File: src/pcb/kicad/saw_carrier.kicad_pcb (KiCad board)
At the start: 2 copper layers, 60.5 x 19.5 mm, 16 parts, among them J1 Conn_Coaxial, J2 Conn_Coaxial, U1 SAW_Sensor

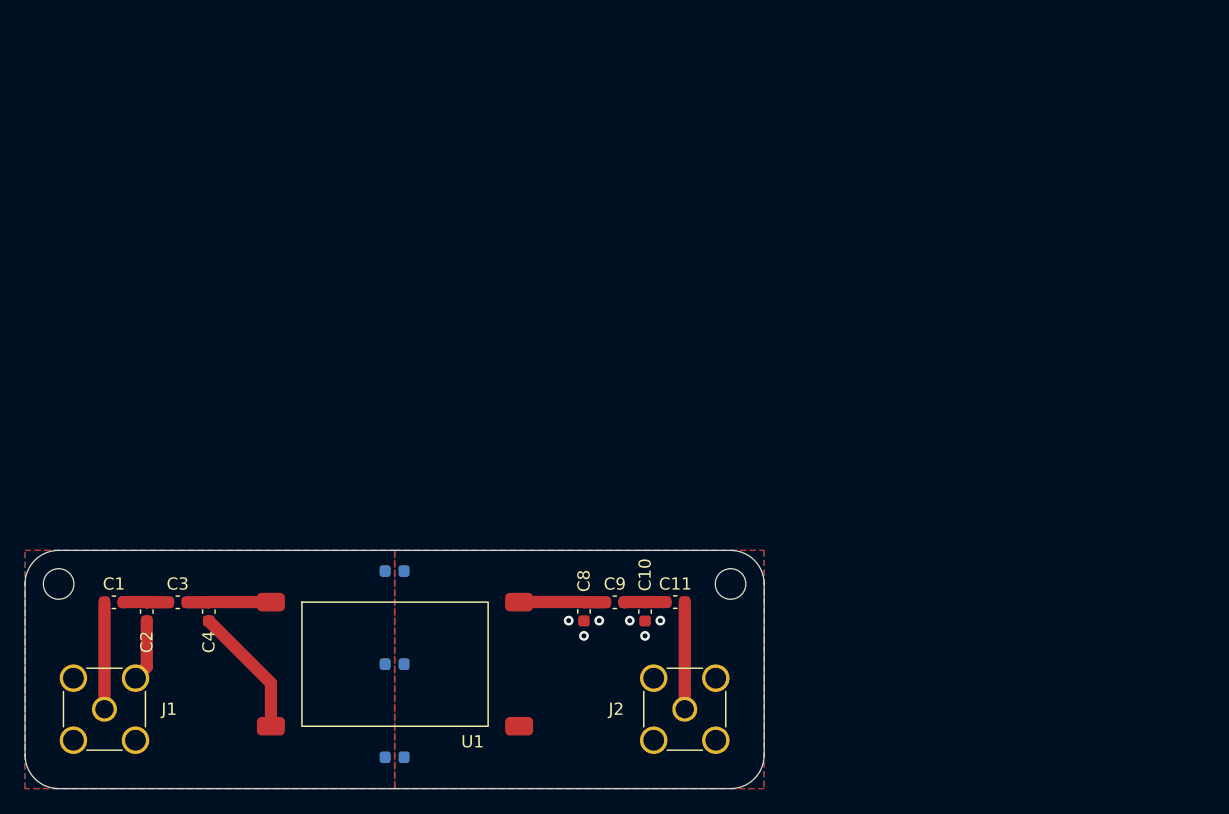
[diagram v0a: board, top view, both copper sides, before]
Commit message: remove obsolete folder
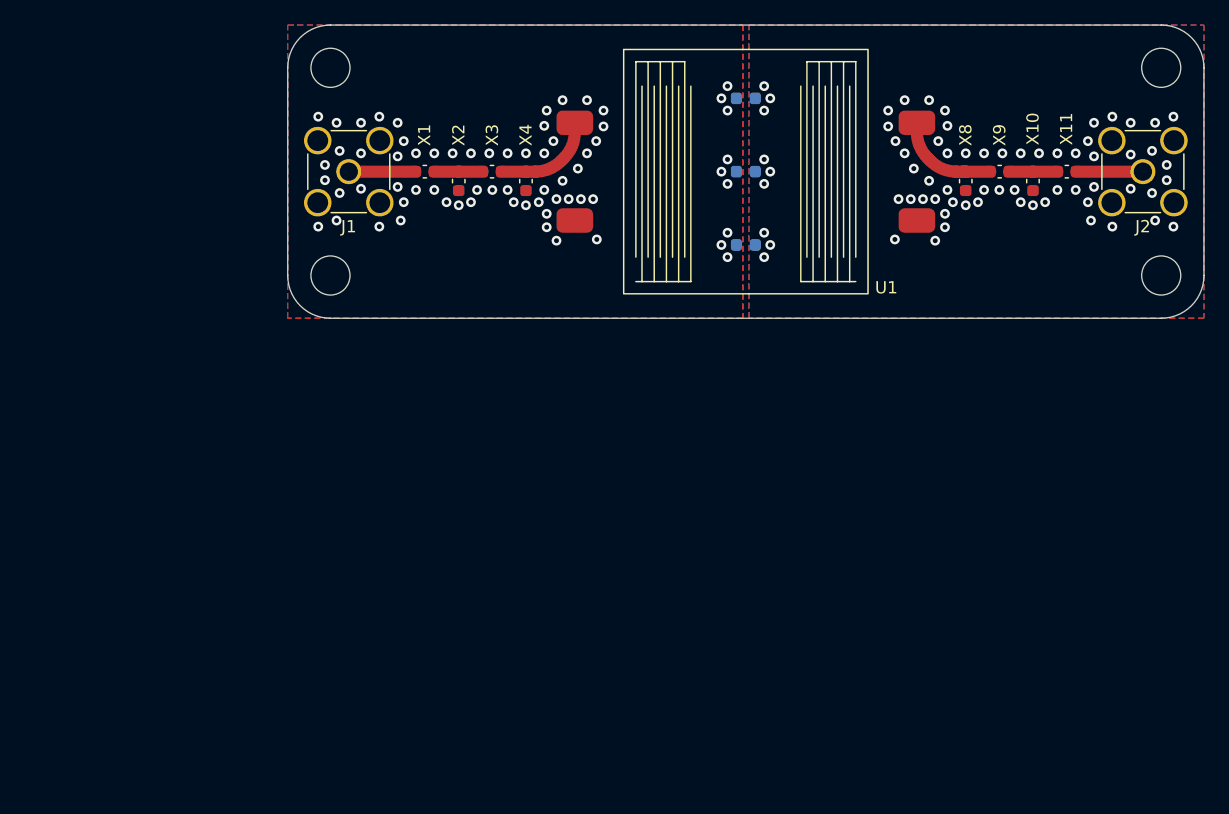
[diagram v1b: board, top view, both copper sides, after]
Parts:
- removed C5: C_Small, Capacitor_SMD:C_0603_1608Metric
- added C1: C_Small, Capacitor_SMD:C_0603_1608Metric, B.Cu at (150.0, 67.0)
- added G1: logo, saw_sensor:hs_wismar_logo_12mmx9_2mm, B.Cu at (142.2, 62.0)
- added G2: logo, saw_sensor:hs_wismar_logo_6_2mmx5mm, F.Cu at (122.8, 58.5)
- added H2: MountingHole, MountingHole:MountingHole_3.2mm_M3, F.Cu at (184.0, 58.5)
- added H4: MountingHole, MountingHole:MountingHole_3.2mm_M3, F.Cu at (184.0, 75.5)
- H1, H3: footprint MountingHole:MountingHole_2.5mm -> MountingHole:MountingHole_3.2mm_M3
- moved C2 61.1 mm to (150.0, 61.0)
- moved J2 57.8 mm to (182.5, 67.0)
- moved U1 49.5 mm to (150.0, 67.0)
- moved J1 48.3 mm to (117.5, 67.0)
- moved H1 47.8 mm to (116.0, 58.5)
- moved X11 47.6 mm to (176.3, 67.0)
- moved X10 47.4 mm to (173.5, 67.8)
- moved X9 47.3 mm to (170.8, 67.0)
- moved X8 47.1 mm to (168.0, 67.8)
- moved C3 44.8 mm to (150.0, 73.0)
- moved X4 43.8 mm to (132.0, 67.8)
- moved X3 43.6 mm to (129.2, 67.0)
- moved X2 43.5 mm to (126.5, 67.8)
- moved X1 43.5 mm to (123.7, 67.0)
- moved H3 41.4 mm to (116.0, 75.5)
- renumbered C6 to C2, C7 to C3, C1 to X1, C10 to X10, C11 to X11, C2 to X2, C3 to X3, C4 to X4, C8 to X8, C9 to X9
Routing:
- net GND1: track 15.8 -> 0.00 mm, vias 0 -> 67
- net /OUT_2: track 8.77 -> 5.45 mm
- net /IN_2: track 8.62 -> 5.45 mm
- net /OUT_0: track 7.07 -> 9.05 mm
- net /IN_0: track 6.85 -> 8.54 mm
- net /OUT_1: track 3.41 -> 3.95 mm
- net GND2: vias 6 -> 67
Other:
- board size 60.5 x 19.5 mm -> 75 x 24 mm
- board text added: "2023"
- board text added: "SAW Carrier Rev. 00.01"
